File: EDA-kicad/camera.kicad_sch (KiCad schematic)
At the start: 3 parts, among them U9 FPC15pin-1mm-pitch-F52Q-1A7H1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

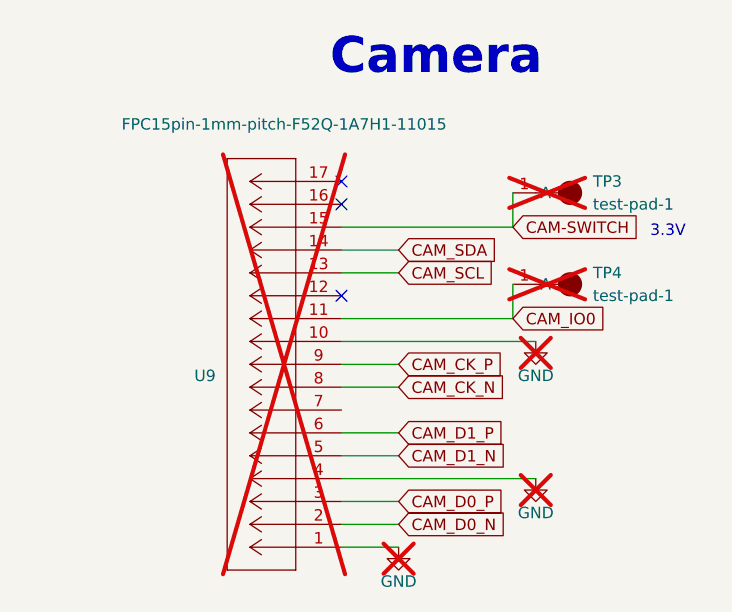
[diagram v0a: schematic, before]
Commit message: reannotate entire schematic
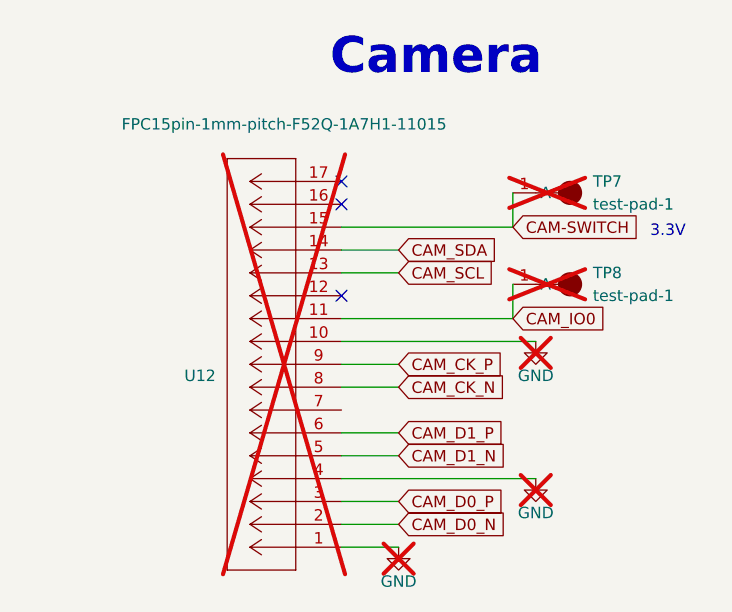
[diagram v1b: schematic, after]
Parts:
- renumbered TP3 to TP7, TP4 to TP8, U9 to U12
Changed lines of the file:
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@@
 		(on_board yes)
 		(dnp yes)
-		(property "Reference" "#PWR0126"
+		(property "Reference" "#PWR0144"
 			(at 151.13 93.98 0)
 			(effects
@@
 			(project "cm5-carrier"
 				(path "/28c5e4fe-1ec7-4477-97f0-d2ec1401fad5/7ec223ba-5b63-4970-8f4e-9b03f0ec9947"
-					(reference "#PWR0126")
+					(reference "#PWR0144")
 					(unit 1)
 				)
@@
 		(on_board yes)
 		(dnp yes)
-		(property "Reference" "#PWR0128"
+		(property "Reference" "#PWR0146"
 			(at 135.89 116.84 0)
 			(effects
@@
 			(project "cm5-carrier"
 				(path "/28c5e4fe-1ec7-4477-97f0-d2ec1401fad5/7ec223ba-5b63-4970-8f4e-9b03f0ec9947"
-					(reference "#PWR0128")
+					(reference "#PWR0146")
 					(unit 1)
 				)
@@
 		(on_board yes)
 		(dnp yes)
-		(property "Reference" "#PWR0127"
+		(property "Reference" "#PWR0145"
 			(at 151.13 109.22 0)
 			(effects
@@
 			(project "cm5-carrier"
 				(path "/28c5e4fe-1ec7-4477-97f0-d2ec1401fad5/7ec223ba-5b63-4970-8f4e-9b03f0ec9947"
-					(reference "#PWR0127")
+					(reference "#PWR0145")
 					(unit 1)
 				)
@@
 		(on_board yes)
 		(dnp yes)
-		(property "Reference" "U9"
+		(property "Reference" "U12"
 			(at 115.57 91.4401 0)
 			(effects
@@
 			(project "cm5-carrier"
 				(path "/28c5e4fe-1ec7-4477-97f0-d2ec1401fad5/7ec223ba-5b63-4970-8f4e-9b03f0ec9947"
-					(reference "U9")
+					(reference "U12")
 					(unit 1)
 				)
@@
 		(dnp yes)
 		(fields_autoplaced yes)
-		(property "Reference" "TP3"
+		(property "Reference" "TP7"
 			(at 157.48 69.8499 0)
 			(effects
@@
 			(project "cm5-carrier"
 				(path "/28c5e4fe-1ec7-4477-97f0-d2ec1401fad5/7ec223ba-5b63-4970-8f4e-9b03f0ec9947"
-					(reference "TP3")
+					(reference "TP7")
 					(unit 1)
 				)
@@
 		(dnp yes)
 		(fields_autoplaced yes)
-		(property "Reference" "TP4"
+		(property "Reference" "TP8"
 			(at 157.48 80.0099 0)
 			(effects
@@
 			(project "cm5-carrier"
 				(path "/28c5e4fe-1ec7-4477-97f0-d2ec1401fad5/7ec223ba-5b63-4970-8f4e-9b03f0ec9947"
-					(reference "TP4")
-					(unit 1)
-				)
+					(reference "TP8")
+					(unit 1)
+				)

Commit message: change some labels
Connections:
- net CAM-SWITCH renamed CAM SWITCH
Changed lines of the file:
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@@
 		)
 	)
-	(global_label "CAM-SWITCH"
+	(global_label "CAM SWITCH"
 		(shape input)
 		(at 148.59 74.93 0)
@@
 		)
 		(property "Intersheetrefs" "${INTERSHEET_REFS}"
-			(at 163.2193 74.8506 0)
+			(at 163.1866 74.93 0)
 			(effects
 				(font
